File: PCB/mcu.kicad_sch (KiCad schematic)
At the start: 29 parts, among them J5 Conn_ST_STDC14, J6 Conn_01x03, J7 Conn_ARM_SWD_TagConnect_TC203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, SW1 SW_Push, U3 STM32F103C8Tx, Y1 ABM3B-8.000MHZ-B2-T

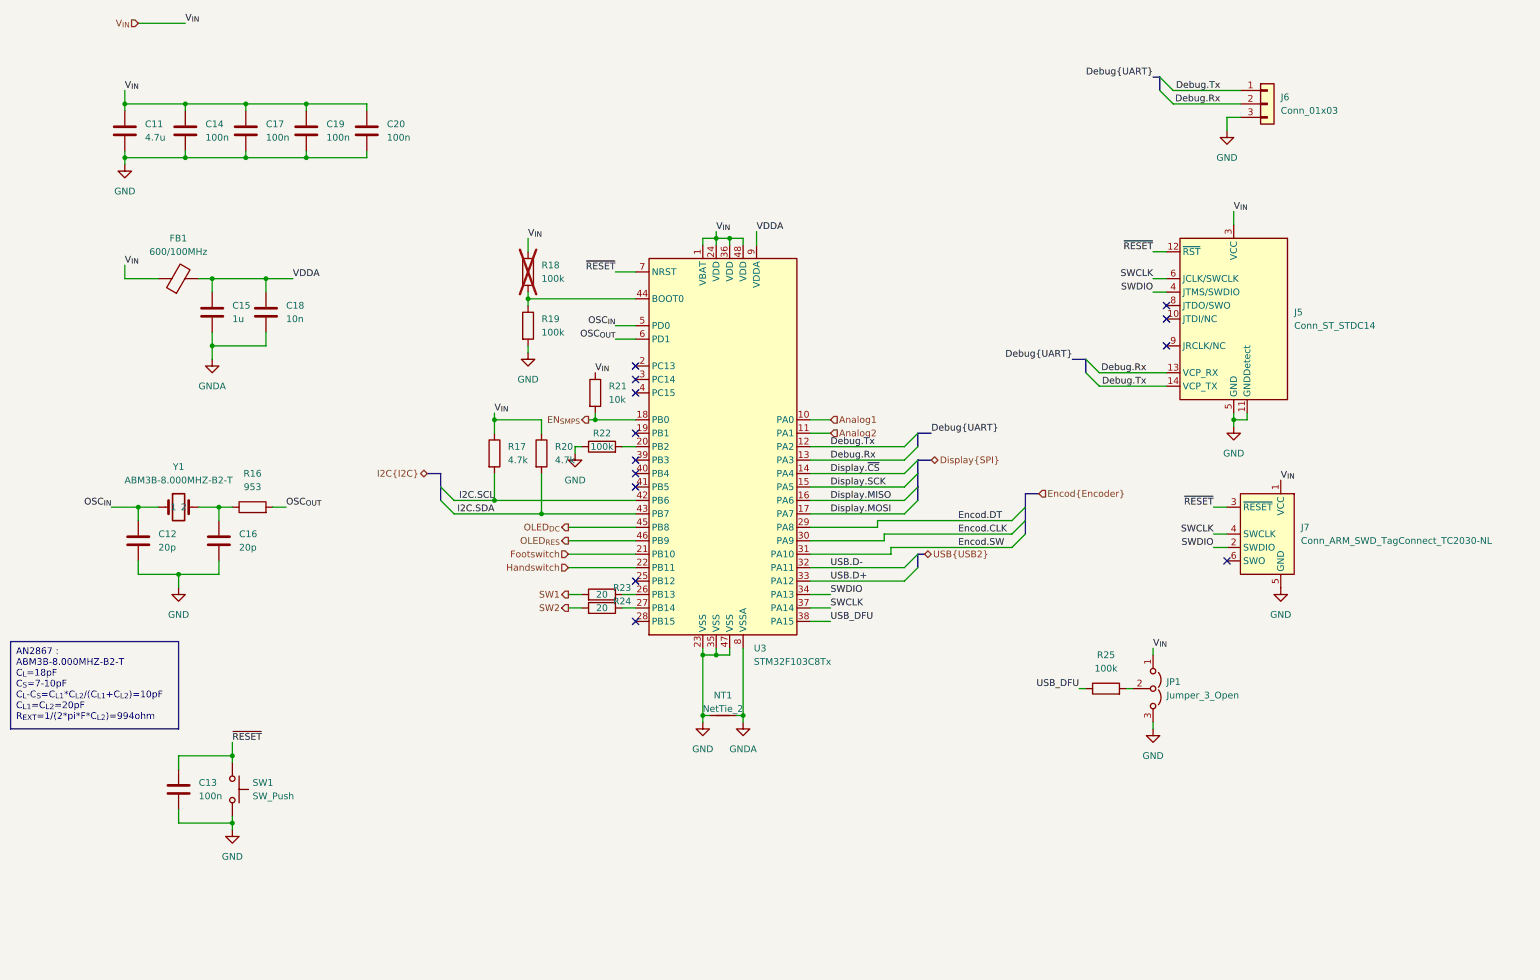
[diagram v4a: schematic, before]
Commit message: schematic done and bom ok
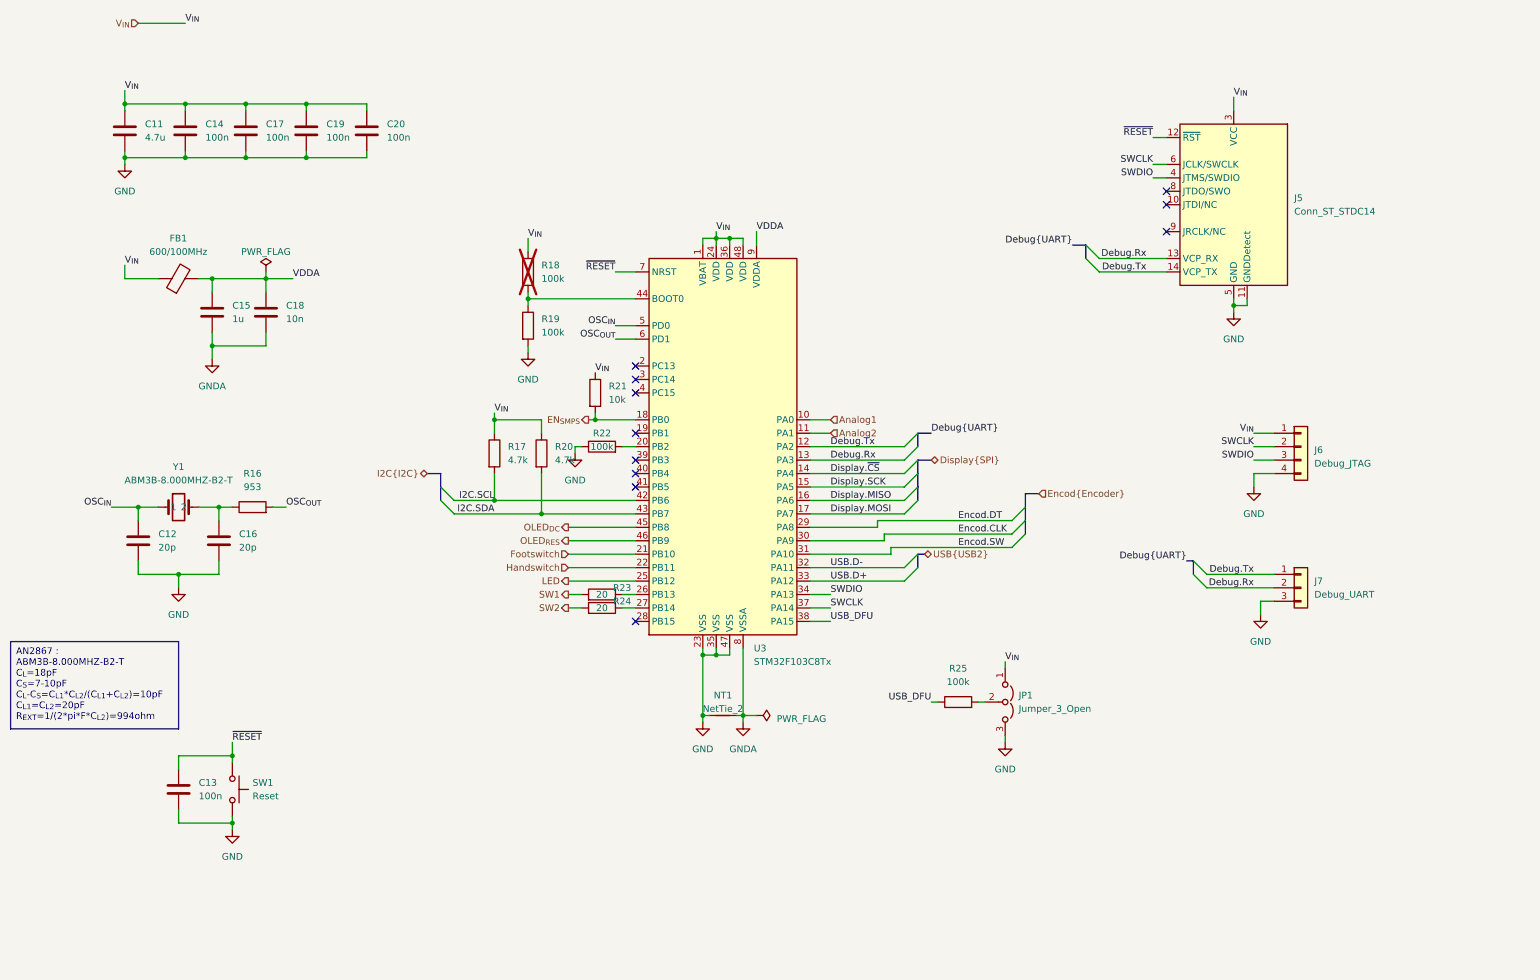
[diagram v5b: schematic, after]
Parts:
- removed J7: Conn_ARM_SWD_TagConnect_TC2030-NL, Connector:Tag-Connect_TC2030-IDC-NL_2x03_P1.27mm_Vertical, symbol Connector:Conn_ARM_SWD_TagConnect_TC2030-NL
- added J6: Debug_JTAG, Connector_PinHeader_2.54mm:PinHeader_1x04_P2.54mm_Vertical, symbol Connector_Generic:Conn_01x04
- J5: footprint (none) -> Connector_PinSocket_1.27mm:PinSocket_2x07_P1.27mm_Vertical_SMD; MPN (none) -> 20021121-00014C1LF; Manufacturer (none) -> Amphenol FCI
- J7: renamed from J6; value Conn_01x03 -> Debug_UART; footprint (none) -> Connector_PinHeader_2.54mm:PinHeader_1x03_P2.54mm_Vertical
- SW1: value SW_Push -> Reset; footprint (none) -> Button_Switch_SMD:SW_SPST_Omron_B3FS-101xP; MPN (none) -> B3FS-1012P; Manufacturer (none) -> Omron
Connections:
- net GND: now also J6.4 (Pin_4)
- net SWCLK: now also J6.2 (Pin_2)
- net SWDIO: now also J6.3 (Pin_3)
- net V_{IN}: now also J6.1 (Pin_1)
- net LED: now reaches U3.25 (PB12)
- no-connect marks 13 -> 11
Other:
- moved on the sheet: J5, J7, JP1, R25

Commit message: add 3d models
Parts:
- J5: footprint Connector_PinSocket_1.27mm:PinSocket_2x07_P1.27mm_Vertical_SMD -> Connector_PinHeader_1.27mm:PinHeader_2x07_P1.27mm_Vertical_SMD
- JP1: footprint (none) -> Connector_PinHeader_2.54mm:PinHeader_1x03_P2.54mm_Vertical
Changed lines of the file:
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@@
     (effects (font (size 1.27 1.27)) (justify left bottom))
   )
-  (label "Display.MISO" (at 167.64 110.49 0)
+  (label "Display.MISO" (at 167.64 110.49 0) (fields_autoplaced)
     (effects (font (size 1.27 1.27)) (justify left bottom))
   )
@@
       (effects (font (size 1.27 1.27)) (justify right))
     )
-    (property "Footprint" "Connector_PinSocket_1.27mm:PinSocket_2x07_P1.27mm_Vertical_SMD" (at 243.84 54.61 0)
+    (property "Footprint" "Connector_PinHeader_1.27mm:PinHeader_2x07_P1.27mm_Vertical_SMD" (at 243.84 54.61 0)
       (effects (font (size 1.27 1.27)) hide)
     )
@@
       (effects (font (size 1.27 1.27)) (justify left))
     )
-    (property "Footprint" "" (at 200.66 148.59 0)
-      (effects (font (size 1.27 1.27)) hide)
-    )
+    (property "Footprint" "Connector_PinHeader_2.54mm:PinHeader_1x03_P2.54mm_Vertical" (at 200.66 148.59 0)
+      (effects (font (size 1.27 1.27)) hide)
+    )

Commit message: ok better cap
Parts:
- SW1: footprint Button_Switch_SMD:SW_SPST_Omron_B3FS-101xP -> Button_Switch_SMD:SW_SPST_EVQP2; MPN B3FS-1012P -> EVQ-P2602W; Manufacturer Omron -> Panasonic
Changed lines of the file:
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@@
       (effects (font (size 1.27 1.27)) (justify left))
     )
-    (property "Footprint" "Button_Switch_SMD:SW_SPST_Omron_B3FS-101xP" (at 59.69 165.1 0)
+    (property "Footprint" "Button_Switch_SMD:SW_SPST_EVQP2" (at 59.69 165.1 0)
       (effects (font (size 1.27 1.27)) hide)
     )
@@
       (effects (font (size 1.27 1.27)) hide)
     )
-    (property "MPN" "B3FS-1012P" (at 54.61 165.1 0)
+    (property "MPN" "EVQ-P2602W" (at 54.61 165.1 0)
       (effects (font (size 1.27 1.27)) hide)
     )
-    (property "Manufacturer" "Omron" (at 54.61 165.1 0)
+    (property "Manufacturer" "Panasonic" (at 54.61 165.1 0)
       (effects (font (size 1.27 1.27)) hide)
     )

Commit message: placement ok
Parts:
- Y1: symbol Device:Crystal -> Device:Crystal_GND24
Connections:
- net GND: now also Y1.2, Y1.4
- net at C16.1, R16.1: now also Y1.3; no longer Y1.2
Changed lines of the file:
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@@
+    (stroke (width 0) (type default))
+  )
+  (wire (pts (xy 44.45 116.84) (xy 44.45 124.46))
     (stroke (width 0) (type default))
   )
@@
     )
   )
+  (symbol (lib_id "power:GND") (at 44.45 106.68 180) (unit 1)
+    (in_bom yes) (on_board yes) (dnp no) (fields_autoplaced)
+    (property "Reference" "#PWR080" (at 44.45 100.33 0)
+      (effects (font (size 1.27 1.27)) hide)
+    )
+    (property "Value" "GND" (at 44.45 102.87 0)
+      (effects (font (size 1.27 1.27)))
+    )
+    (property "Footprint" "" (at 44.45 106.68 0)
+      (effects (font (size 1.27 1.27)) hide)
+    )
+    (property "Datasheet" "" (at 44.45 106.68 0)
+      (effects (font (size 1.27 1.27)) hide)
+    )
+    (pin "1")
+    (instances
+      (project "Tattoo_Supply"
+        (path "/036b57f3-323c-4da7-bad2-1c27fa1415e1/fd65dc63-1d27-4821-ae4f-326fe3a44815"
+          (reference "#PWR080") (unit 1)
+        )
+      )
+    )
+  )
   (symbol (lib_id "power:GND") (at 119.38 101.6 0) (unit 1)
     (in_bom yes) (on_board yes) (dnp no) (fields_autoplaced)
@@
     )
   )
-  (symbol (lib_id "Device:Crystal") (at 44.45 111.76 0) (unit 1)
-    (in_bom yes) (on_board yes) (dnp no) (fields_autoplaced)
-    (property "Reference" "Y1" (at 44.45 104.14 0)
-      (effects (font (size 1.27 1.27)))
-    )
-    (property "Value" "ABM3B-8.000MHZ-B2-T" (at 44.45 106.68 0)
+  (symbol (lib_id "Device:Crystal_GND24") (at 44.45 111.76 0) (unit 1)
+    (in_bom yes) (on_board yes) (dnp no)
+    (property "Reference" "Y1" (at 44.45 97.79 0)
+      (effects (font (size 1.27 1.27)))
+    )
+    (property "Value" "ABM3B-8.000MHZ-B2-T" (at 44.45 100.33 0)
       (effects (font (size 1.27 1.27)))
     )
@@
     (pin "1")
     (pin "2")
+    (pin "3")
+    (pin "4")
     (instances
       (project "Tattoo_Supply"
@@
   )
   (symbol (lib_id "Device:C") (at 36.83 118.11 0) (unit 1)
-    (in_bom yes) (on_board yes) (dnp no) (fields_autoplaced)
-    (property "Reference" "C12" (at 40.64 116.8399 0)
-      (effects (font (size 1.27 1.27)) (justify left))
-    )
-    (property "Value" "20p" (at 40.64 119.3799 0)
-      (effects (font (size 1.27 1.27)) (justify left))
-    )
+    (in_bom yes) (on_board yes) (dnp no)
+    (property "Reference" "C12" (at 29.21 116.84 0)
+      (effects (font (size 1.27 1.27)) (justify left))
+    )
+    (property "Value" "20p" (at 29.21 119.38 0)
+      (effects (font (size 1.27 1.27)) (justify left))
+    )
